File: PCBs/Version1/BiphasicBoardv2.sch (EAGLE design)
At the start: 17 parts

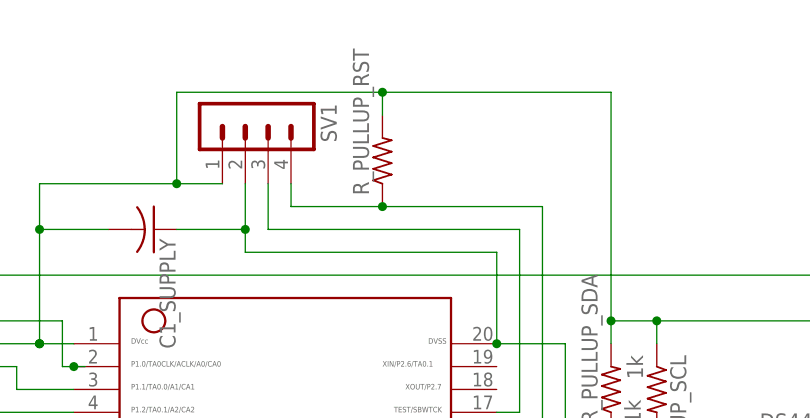
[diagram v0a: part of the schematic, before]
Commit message: Fixed error just introduced in CAM job. Further added values. Labels for power.
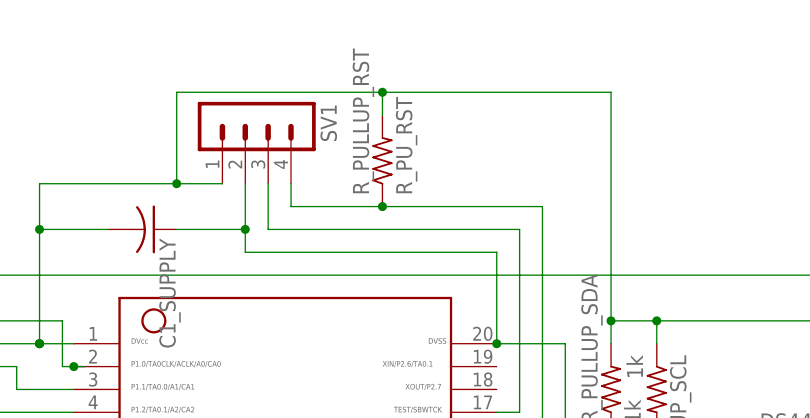
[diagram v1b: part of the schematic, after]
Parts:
- R_PULLUP_RST: value (none) -> R_PU_RST
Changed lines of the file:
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@@
 <part name="R_PULLUP_SDA" library="BiphasicBoard" deviceset="R-US_" device="R0603" value="1k"/>
 <part name="R_INPUT_FS0" library="BiphasicBoard" deviceset="R-US_" device="R0603" value="47k"/>
-<part name="R_PULLUP_RST" library="BiphasicBoard" deviceset="R-US_" device="R0603"/>
+<part name="R_PULLUP_RST" library="BiphasicBoard" deviceset="R-US_" device="R0603" value="R_PU_RST"/>
 <part name="DS4432U+" library="BiphasicBoard" deviceset="DS4432U+" device=""/>
 <part name="MSP430" library="BiphasicBoard" deviceset="MSP430" device=""/>
